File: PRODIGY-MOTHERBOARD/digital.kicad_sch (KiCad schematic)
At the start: 75 parts, among them Q3 BC850, Q4 BS870, Q5 BC850, SW3 SW_Push, SW4 SW_Push, SW5 SW_Push, SW7 SW_Push, U23 SN74LVC1T45DBV, U24 TSDP341xx

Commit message: Submitted V0 for evaluation. Avaiting feedback.
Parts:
- R59: renamed from R58; value 1k -> 10k
- R64: renamed from R63; value 1k -> 4.7k
- renumbered D16 to D36, D17 to D37, D19 to D38, D20 to D39, D21 to D40, D22 to D41, D23 to D42, D24 to D43, D25 to D44, D26 to D45, D27 to D46, D28 to D47, D29 to D48, D30 to D49, D31 to D50, D32 to D51, D33 to D52, D34 to D53, D35 to D54, D36 to D55, D37 to D56, D38 to D57, D39 to D58, D40 to D59, D41 to D60, D42 to D61, JP7 to JP10, R49 to R50, R50 to R51, R51 to R52, R52 to R53, R53 to R54, R54 to R55, R55 to R56, R56 to R57, R57 to R58, R59 to R60, R60 to R61, R61 to R62, R62 to R63, R64 to R65, R65 to R66, R66 to R67, R67 to R68, R68 to R69, R69 to R70, R70 to R71, R71 to R72, R72 to R73, SW7 to SW3, SW3 to SW4, SW4 to SW6, U23 to U24, U24 to U25

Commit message: Finished v0.1 schematic.
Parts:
- renumbered C70 to C67, C71 to C68, C72 to C69, C73 to C70, C74 to C71, C82 to C72, C75 to C73, C76 to C74, C77 to C75, C80 to C76, C78 to C77, C81 to C78, D53 to D39, D57 to D40, D60 to D41, D46 to D42, D61 to D43, D47 to D44, D40 to D45, D48 to D46, D41 to D47, D52 to D48, D56 to D49, D59 to D50, D49 to D51, D42 to D52, D43 to D53, D58 to D54, D50 to D55, D44 to D56, D38 to D57, D36 to D58, D54 to D59, D55 to D60, D51 to D61, D39 to D62, D45 to D63, D37 to D64, JP10 to JP8, Q5 to Q3, Q3 to Q5, R59 to R41, R64 to R42, R69 to R43, R73 to R44, R72 to R45, R58 to R46, R63 to R47, R68 to R48, R71 to R49, R70 to R50, R61 to R51, R66 to R52, R54 to R53, R50 to R54, R56 to R55, R67 to R56, R52 to R57, R55 to R58, R51 to R59, R62 to R61, R65 to R62, R57 to R63, R53 to R64, SW5 to SW3, SW3 to SW4, SW6 to SW5, SW4 to SW6, U24 to U19, U25 to U20

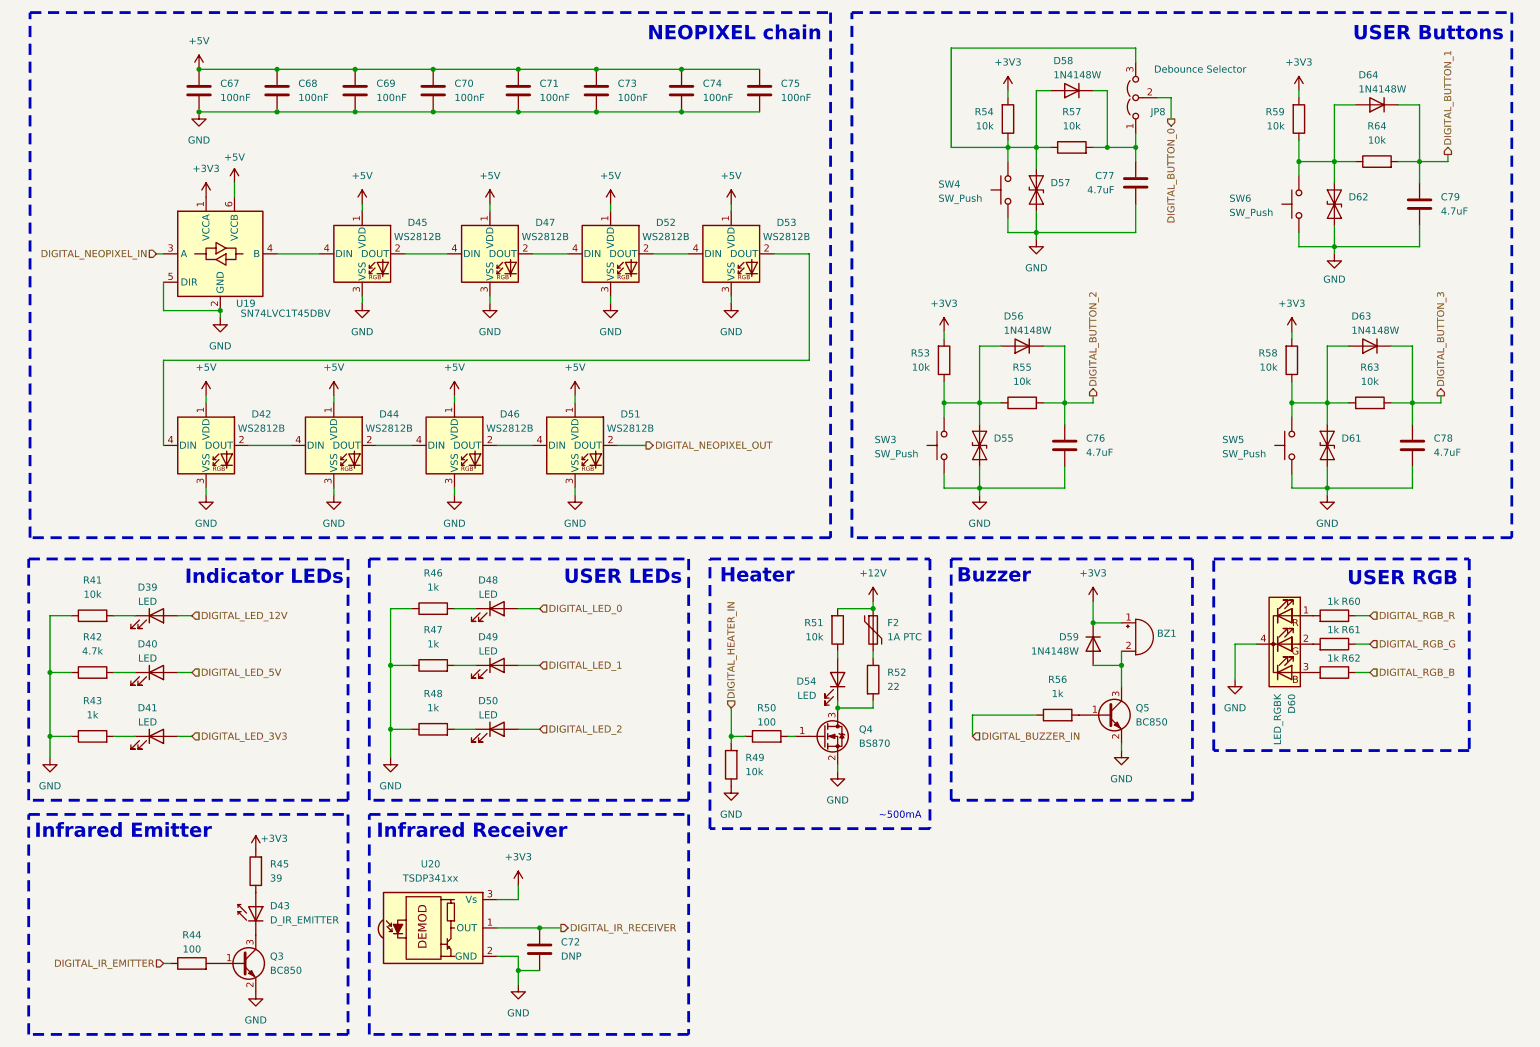
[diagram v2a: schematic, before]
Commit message: MBT Schematic improved
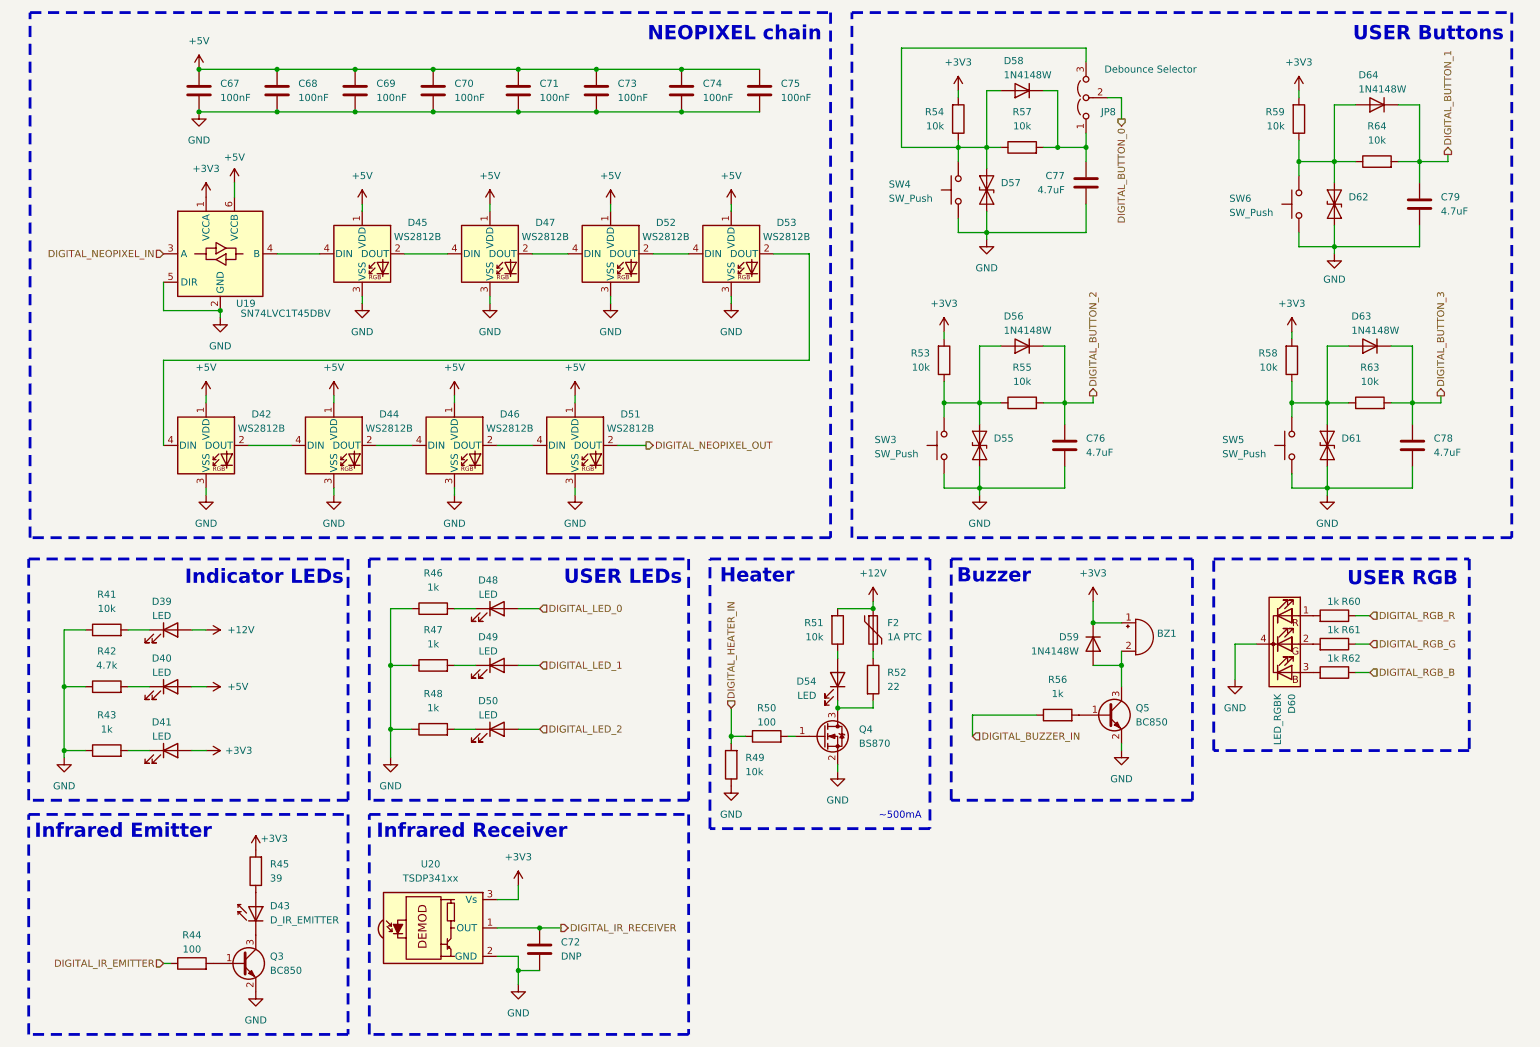
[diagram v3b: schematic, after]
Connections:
- net DIGITAL_LED_12V is gone; now on net +12V: D39.2 (A)
- net DIGITAL_LED_3V3 is gone; now on net +3V3: D41.2 (A)
- net DIGITAL_LED_5V is gone; now on net +5V: D40.2 (A)
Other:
- moved on the sheet: C77, D39, D40, D41, D57, D58, JP8, R41, R42, R43, R54, R57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

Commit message: schematic v0.2 finalized
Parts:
- renumbered C67 to C64, C68 to C65, C69 to C66, C70 to C67, C71 to C68, C72 to C69, C73 to C70, C74 to C71, C75 to C72, C76 to C73, C77 to C74, C78 to C75, C79 to C76, D57 to D56, D58 to D57, D56 to D58, JP8 to JP9, Q3 to Q2, Q4 to Q3, Q5 to Q4, R41 to R38, R42 to R39, R43 to R40, R44 to R41, R45 to R42, R46 to R43, R47 to R44, R48 to R45, R49 to R46, R50 to R47, R51 to R48, R52 to R49, R53 to R50, R54 to R51, R57 to R52, R55 to R53, R56 to R54, R58 to R55, R59 to R56, R60 to R57, R61 to R58, R62 to R59, R63 to R60, R64 to R61, U19 to U18, U20 to U19

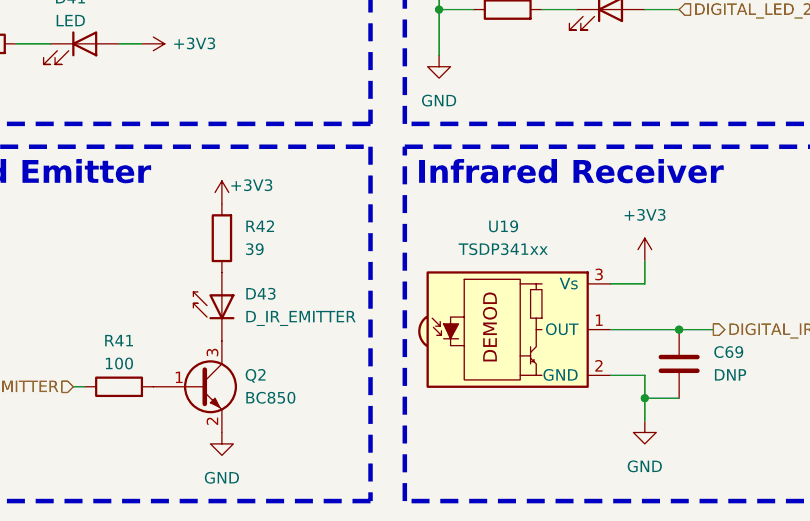
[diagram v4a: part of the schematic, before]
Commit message: changed breakout connectors and bpc size
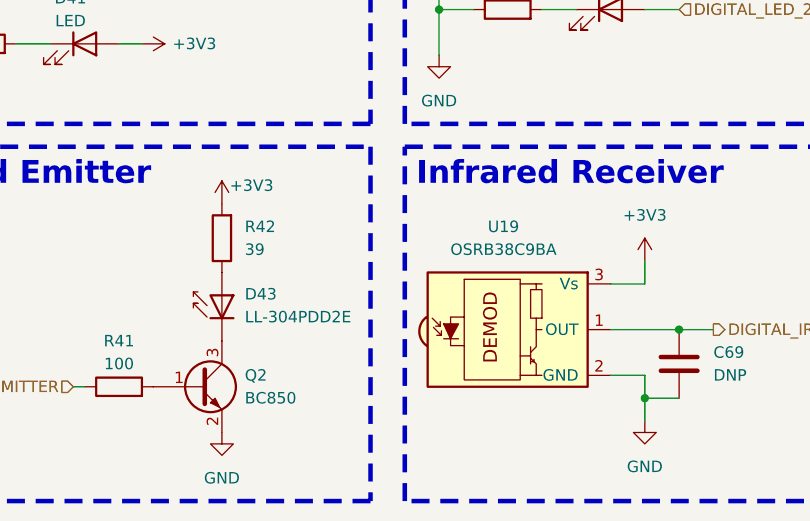
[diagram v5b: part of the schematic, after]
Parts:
- D43: value D_IR_EMITTER -> LL-304PDD2E; footprint LED_THT:LED_D5.0mm_Horizontal_O1.27mm_Z3.0mm_Clear -> LED_THT:LED_D3.0mm_Horizontal_O1.27mm_Z2.0mm_IRBlack
- U19: value TSDP341xx -> OSRB38C9BA
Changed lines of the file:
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@@
 			)
 		)
-		(property "Value" "D_IR_EMITTER"
+		(property "Value" "LL-304PDD2E"
 			(at 58.42 176.4029 90)
 			(effects
@@
 			)
 		)
-		(property "Footprint" "LED_THT:LED_D5.0mm_Horizontal_O1.27mm_Z3.0mm_Clear"
+		(property "Footprint" "LED_THT:LED_D3.0mm_Horizontal_O1.27mm_Z2.0mm_IRBlack"
 			(at 51.435 173.99 0)
 			(effects
@@
 			)
 		)
-		(property "Datasheet" "http://www.osram-os.com/Graphics/XPic0/00203825_0.pdf"
+		(property "Datasheet" "https://www.tme.eu/hu/details/ll-304pdd2e/fotodiodak/luckylight/"
 			(at 55.88 175.26 0)
 			(effects
@@
 			)
 		)
-		(property "Value" "TSDP341xx"
+		(property "Value" "OSRB38C9BA"
 			(at 87.165 168.91 0)
 			(effects
@@
 			)
 		)
-		(property "Datasheet" "http://www.vishay.com/docs/82667/tsdp341.pdf"
+		(property "Datasheet" "https://www.tme.eu/hu/details/osrb38c9ba/ir-vevo-modulok/optosupply/"
 			(at 105.41 170.18 0)
 			(effects

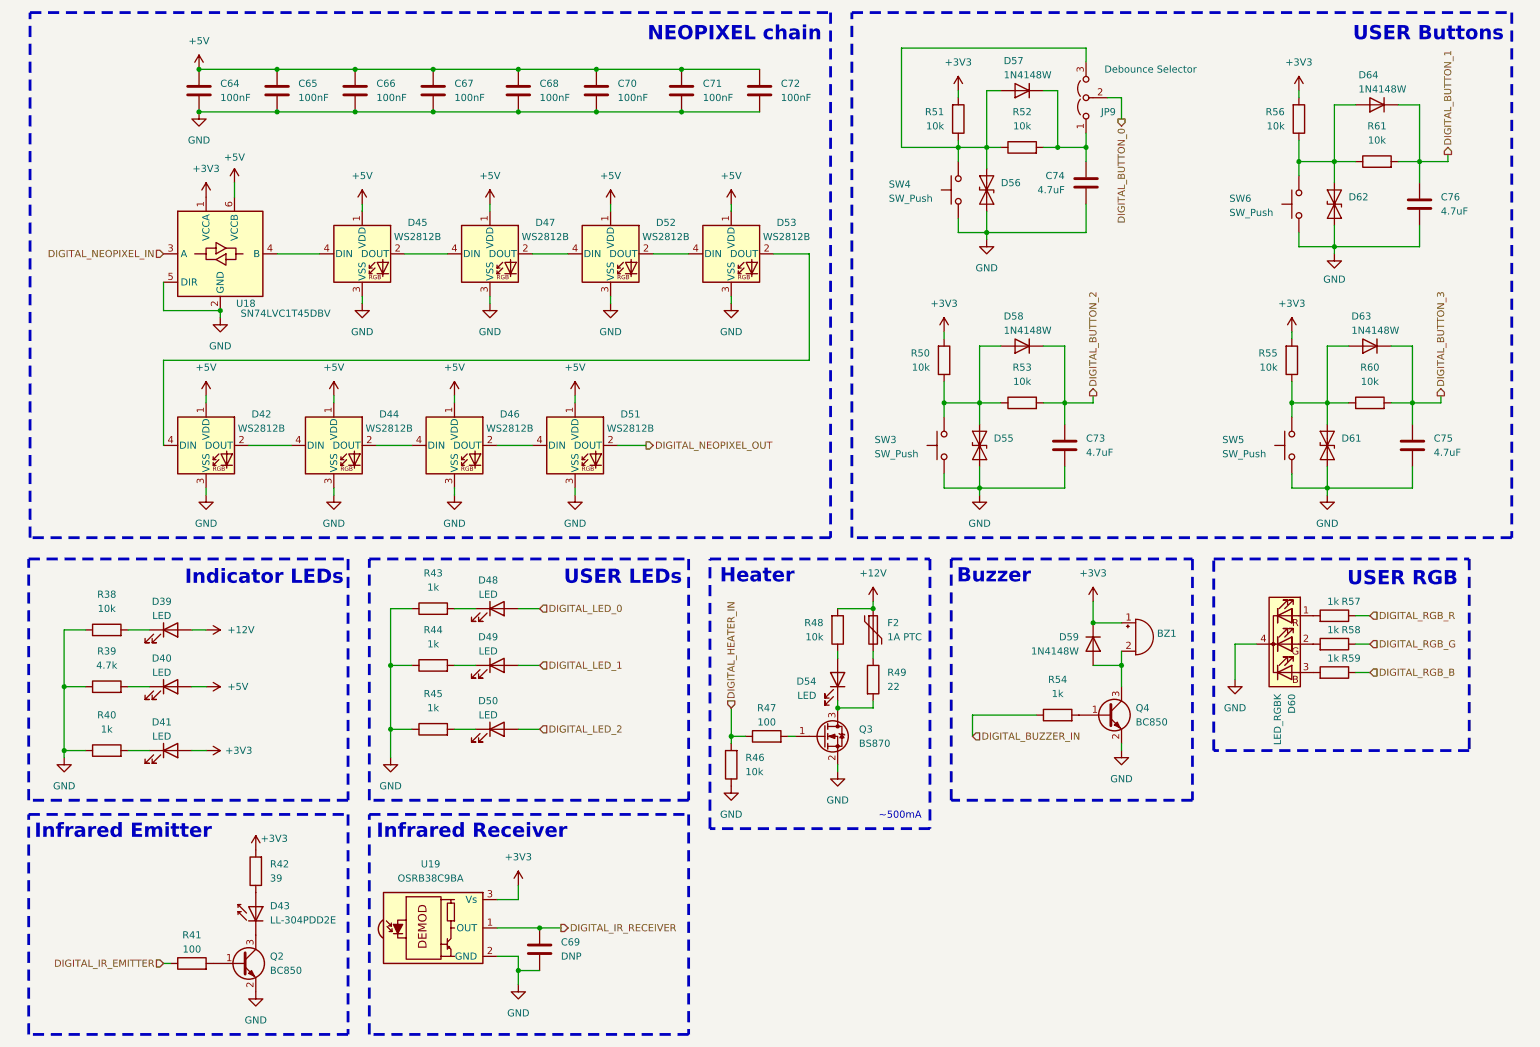
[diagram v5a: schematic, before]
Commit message: Motherboard footprints assigned.
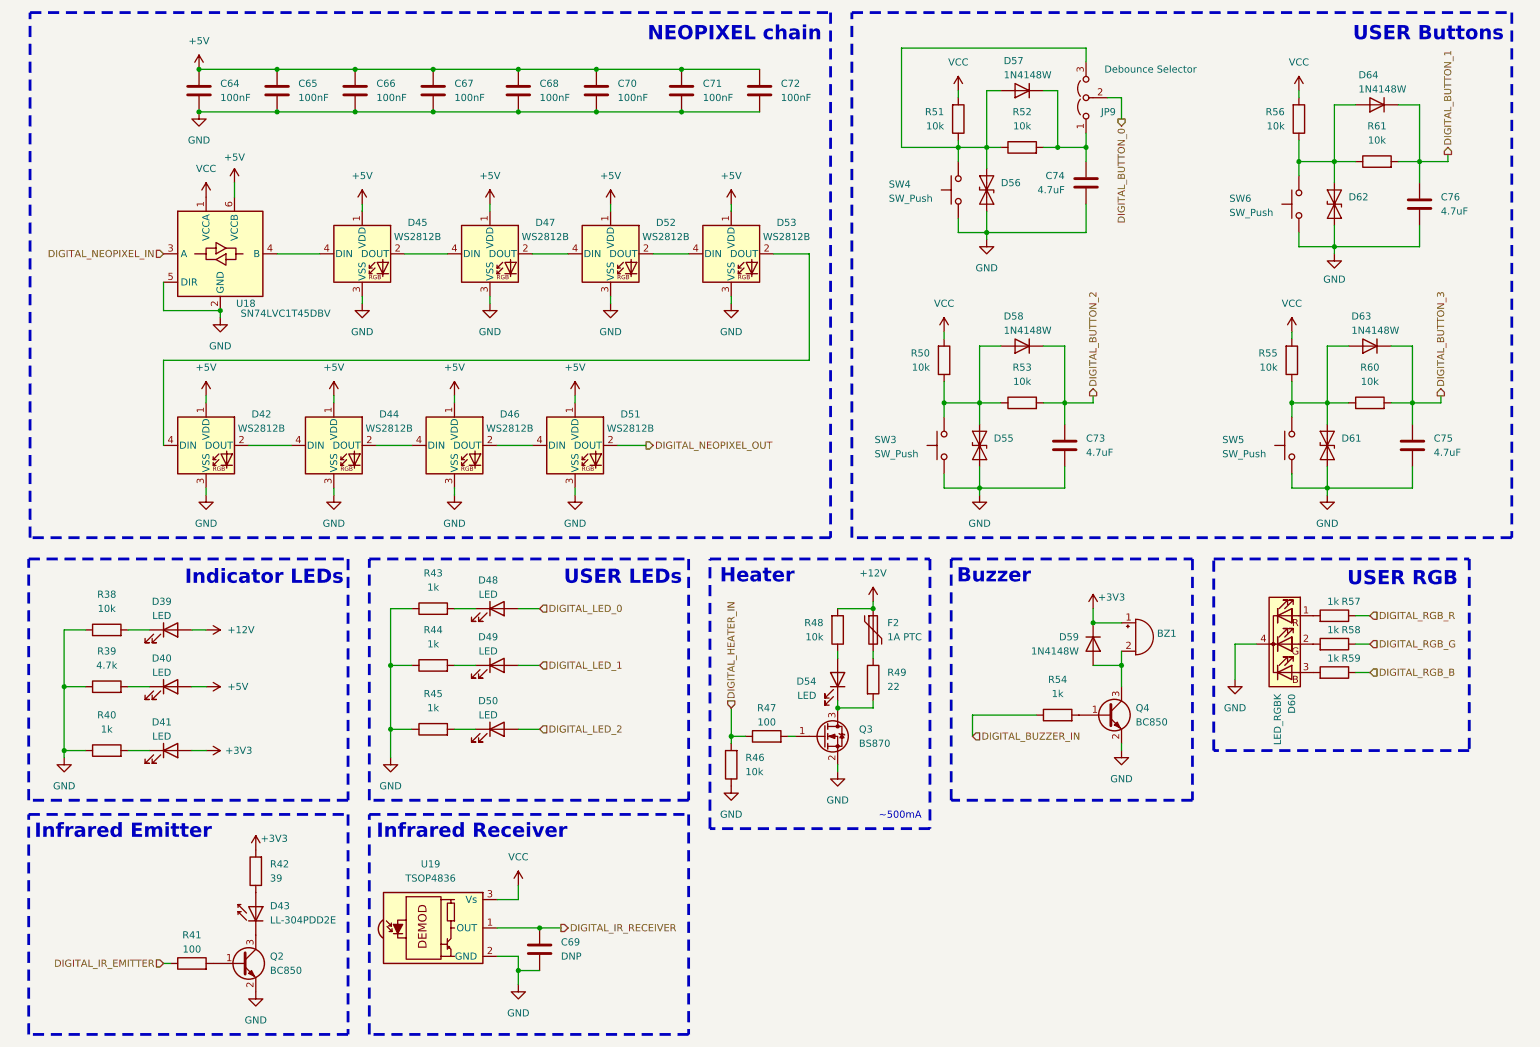
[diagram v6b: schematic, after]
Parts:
- BZ1: footprint Buzzer_Beeper:Buzzer_Mallory_AST1240MLQ -> Buzzer_Beeper:MagneticBuzzer_Kobitone_254-EMB84Q-RO; MOUSER (none) -> 490-CMT-9504-87SMTTR
- C64, C65, C66, C67, C68, C70, C71, C72: footprint (none) -> Capacitor_SMD:C_0603_1608Metric
- C69: footprint (none) -> Resistor_SMD:R_0603_1608Metric
- C73, C75, C76: footprint Capacitor_SMD:C_0603_1608Metric -> Capacitor_SMD:C_0805_2012Metric
- C74: footprint (none) -> Capacitor_SMD:C_0805_2012Metric
- D60: footprint (none) -> LED_THT:LED_D5.0mm-4_RGB
- JP9: footprint (none) -> Connector_PinHeader_2.54mm:PinHeader_1x03_P2.54mm_Vertical
- R42: footprint Resistor_SMD:R_0603_1608Metric -> Resistor_SMD:R_0805_2012Metric
- U19: value OSRB38C9BA -> TSOP4836; TME (none) -> TSOP4836
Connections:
- net +3V3: no longer R50.2, R51.2, R55.2, R56.2, U18.1 (VCCA), U19.3 (Vs)
- new net VCC: R50.2, R51.2, R55.2, R56.2, U18.1 (VCCA), U19.3 (Vs)
